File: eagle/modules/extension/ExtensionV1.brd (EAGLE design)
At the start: 113 x 82.5 mm, 4 parts, among them IC1 LM3940IS-3.3F

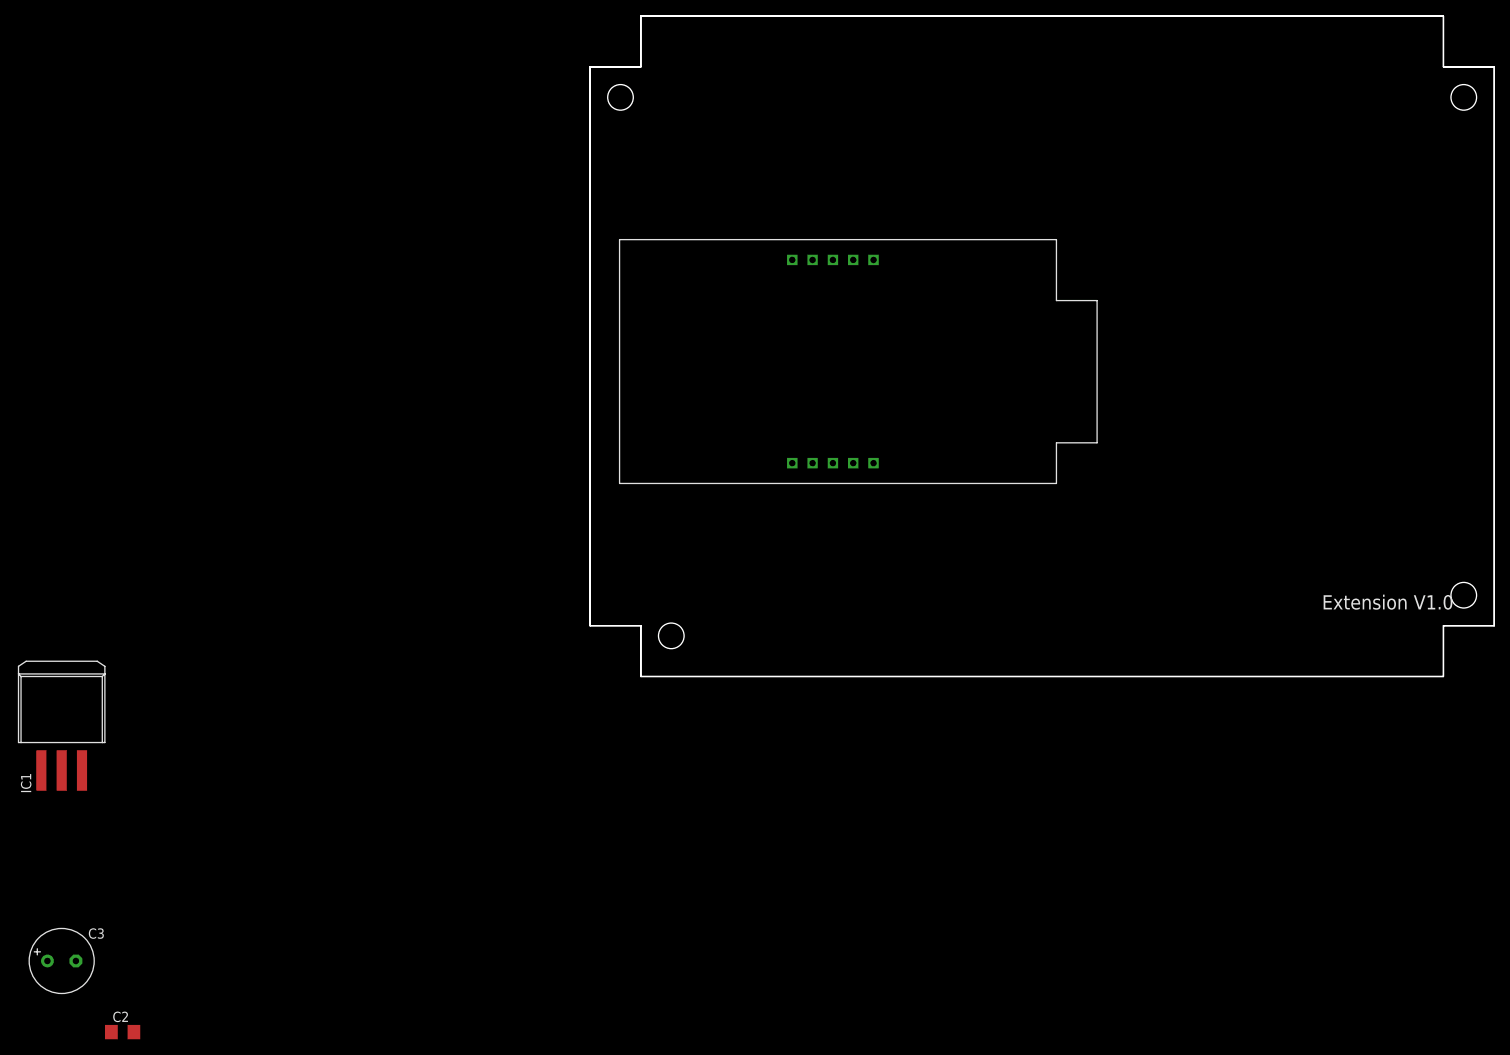
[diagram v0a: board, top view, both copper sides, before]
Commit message: Update extension and create new nano I2C
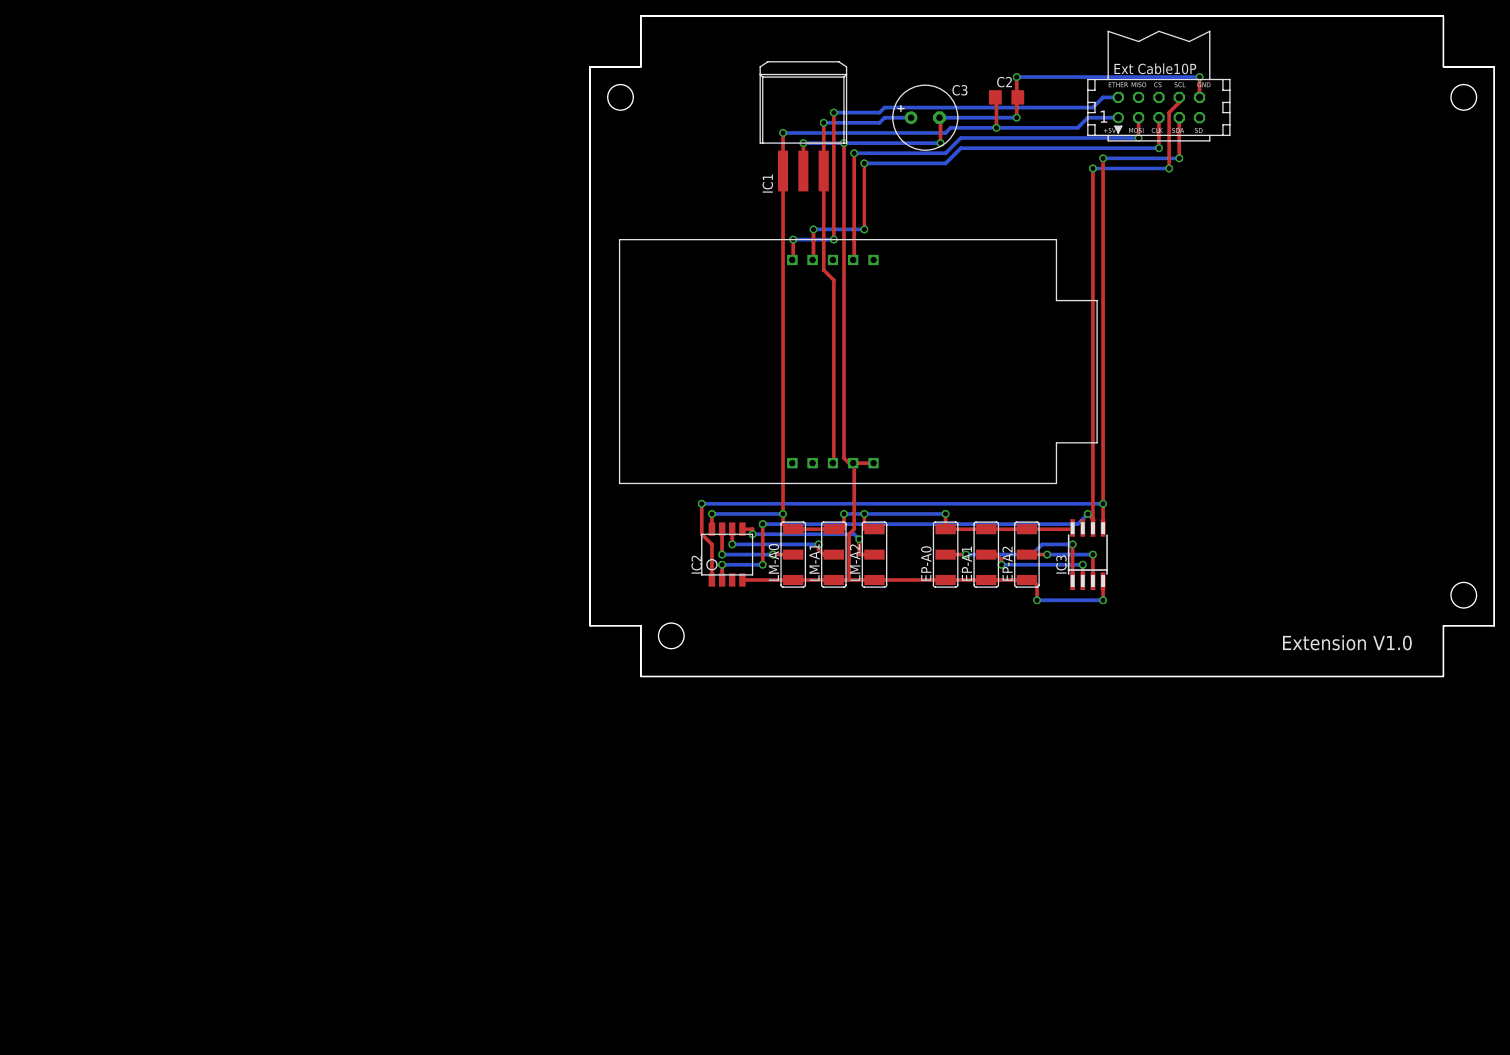
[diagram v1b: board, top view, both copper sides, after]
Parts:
- added CON1: (no value), lpatiny:CON10EXT
- added EP-A0, EP-A1, EP-A2, LM-A0, LM-A1, LM-A2: (no value), lpatiny:1206-SWITCH
- added IC2: (no value), lm75:SO8_LM75
- added IC3: 24-C32SM, microchip:SO-08M
- moved C2 160.8 mm to (50.8, 72.4)
- moved C3 150.9 mm to (40.6, 69.8)
- moved IC1 119.2 mm to (25.4, 71.1)
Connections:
- removed net 3.3V: U$1.3.3V
- new net CLK: CON1.CLK, U$1.SCK
- new net CS: U$1.CS
- new net EN_ETH: CON1.EN_ETH, U$1.EN
- new net EN_SD: CON1.EN_SD
- new net MISO: U$1.MISO
- new net MOSI: CON1.MOSI, U$1.MOSI
- new net MSIO: CON1.MISO
- new net N$1: IC2.7, LM-A0.2
- new net N$2: IC2.6, LM-A1.2
- new net N$3: IC2.5, LM-A2.2
- new net N$4: EP-A0.2, IC3.1
- new net N$5: CON1.CS
- new net N$6: EP-A1.2, IC3.2
- new net N$7: EP-A2.2, IC3.3
- new net SCL: CON1.SCL, IC2.2, IC3.6
- new net SDA: CON1.SDA, IC2.1, IC3.5
- net +3V3: now also U$1.3.3V
- net +5V: now also CON1.+5V, EP-A0.3, EP-A1.3, EP-A2.3, IC2.8, IC3.8, LM-A0.3, LM-A1.3, LM-A2.3
- net GND: now also CON1.GND, EP-A0.1, EP-A1.1, EP-A2.1, IC2.4, IC3.4, LM-A0.1, LM-A1.1, LM-A2.1, U$1.GND1, U$1.GND2
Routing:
- net GND: track 0.00 -> 172.0 mm, vias 0 -> 8
- net +5V: track 0.00 -> 149.9 mm, vias 0 -> 7
- net SDA: track 0.00 -> 121.0 mm, vias 0 -> 4
- net SCL: track 0.00 -> 118.0 mm, vias 0 -> 6
- net EN_ETH: track 0.00 -> 60.0 mm, vias 0 -> 3
- net CLK: track 0.00 -> 60.0 mm, vias 0 -> 4
- net +3V3: track 0.00 -> 54.4 mm, vias 0 -> 1
- net MOSI: track 0.00 -> 52.3 mm, vias 0 -> 2
- net N$4: track 0.00 -> 21.0 mm, vias 0 -> 2
- net N$3: track 0.00 -> 19.3 mm, vias 0 -> 2
- net N$2: track 0.00 -> 15.5 mm, vias 0 -> 2
- net N$6: track 0.00 -> 15.0 mm, vias 0 -> 2
- net N$1: track 0.00 -> 12.1 mm, vias 0 -> 2
- net N$7: track 0.00 -> 11.6 mm, vias 0 -> 2

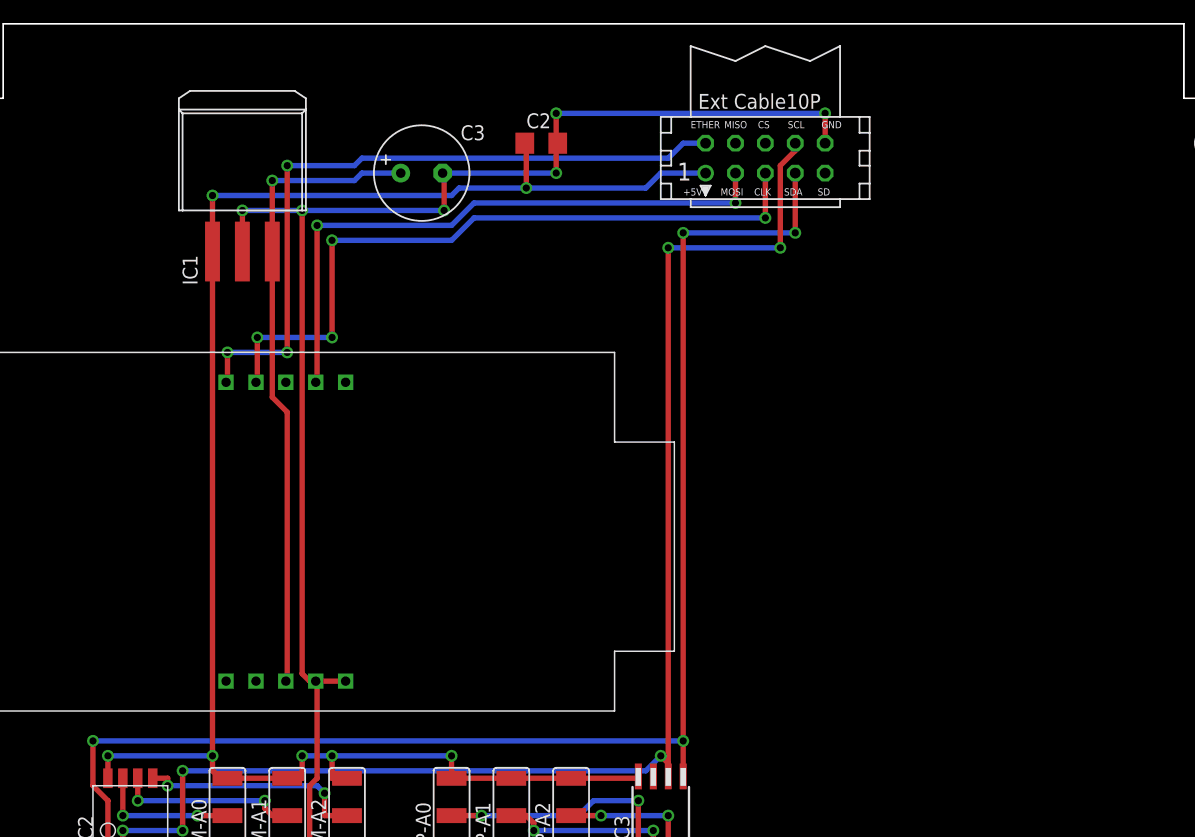
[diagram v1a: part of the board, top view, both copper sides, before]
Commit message: New version of extension, creation of NanoEthernet (draft)
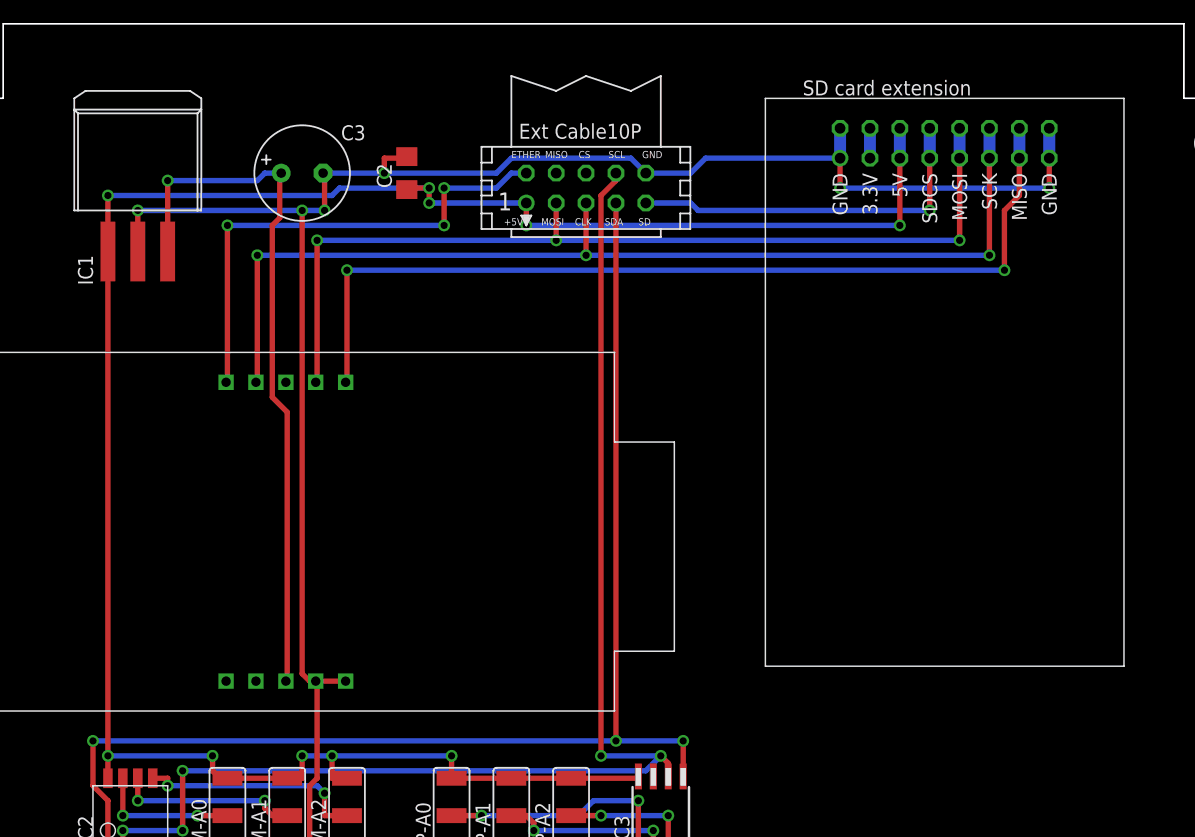
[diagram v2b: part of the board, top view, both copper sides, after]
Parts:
- added CON2: (no value), lpatiny:SD-CARD
- moved CON1 15.5 mm to (54.6, 68.6)
- moved C2 11.7 mm to (39.4, 69.8), turned to 90 degrees
- moved C3 10.2 mm to (30.5, 69.8)
- moved IC1 8.89 mm to (16.5, 71.1)
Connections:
- new net N$14: CON2.3.3V
- net +5V: now also CON2.5V
- net CLK: now also CON2.SCK
- net EN_SD: now also CON2.SDCS
- net GND: now also CON2.GND1, CON2.GND2
- net MISO: now also CON2.MISO
- net MOSI: now also CON2.MOSI
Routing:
- net MISO: track 0.00 -> 75.6 mm, vias 0 -> 2
- net +5V: track 149.9 -> 181.8 mm, vias 7 -> 10
- net GND: track 172.0 -> 202.2 mm
- net EN_SD: track 0.00 -> 28.8 mm, vias 0 -> 1
- net CLK: track 60.0 -> 85.8 mm, vias 4 -> 3
- net MOSI: track 52.3 -> 77.0 mm, vias 2 -> 3
- net EN_ETH: track 60.0 -> 42.6 mm
- net SDA: track 121.0 -> 109.0 mm, vias 4 -> 3
- net SCL: track 118.0 -> 110.4 mm, vias 6 -> 5
- net +3V3: track 54.4 -> 60.2 mm
